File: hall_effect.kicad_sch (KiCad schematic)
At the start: 0 parts

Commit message: added MCU decaps and hall effect schematic
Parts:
- added R3 (x2), R4 (x2): 1.9k, symbol Device:R
- added R5, R6: 22k, symbol Device:R
- added R7: 1k, symbol Device:R
- added R8: 3.6k, symbol Device:R
- added U2, U4: OPA196xDGK, Package_SO:VSSOP-8_3x3mm_P0.65mm, symbol Amplifier_Operational:OPA196xDGK
- added U3: SM351LT, Package_TO_SOT_SMD:SOT-23, symbol Sensor_Magnetic:SM351LT
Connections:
- new net: R7.2, R8.2, U4.2 (-)
- new net: R3.1, R5.2, R6.1
- new net: R3.1, R3.2, U2.2 (-)
- new net: R4.1, R4.1, U2.3 (+)
- new net: R3.2, U2.6, U4.3 (+)
- new net: R4.2, U3.2 (OUTPUT)
- new net +3.3V: R5.1, U3.1 (VCC)
- new net +5V: U2.7 (V+), U4.7 (V+)
- new net ADC_IN1: R8.1, U4.6
- new net GND: R4.2, R6.2, R7.1, U2.4 (V-), U3.3 (GND), U4.4 (V-)

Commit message: layout
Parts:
- R11: renamed from R3; footprint (none) -> Resistor_SMD:R_0805_2012Metric
- R12: renamed from R4; footprint (none) -> Resistor_SMD:R_0805_2012Metric
- R3, R4, R5, R6, R7, R8: footprint (none) -> Resistor_SMD:R_0805_2012Metric
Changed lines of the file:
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@@
 			)
 		)
-		(property "Footprint" ""
+		(property "Footprint" "Resistor_SMD:R_0805_2012Metric"
 			(at 161.29 82.042 90)
 			(effects
@@
 			)
 		)
-		(property "Footprint" ""
+		(property "Footprint" "Resistor_SMD:R_0805_2012Metric"
 			(at 75.692 87.63 90)
 			(effects
@@
 		(dnp no)
 		(fields_autoplaced yes)
-		(property "Reference" "R3"
+		(property "Reference" "R11"
 			(at 91.44 76.2 90)
 			(effects
@@
 			)
 		)
-		(property "Footprint" ""
+		(property "Footprint" "Resistor_SMD:R_0805_2012Metric"
 			(at 91.44 84.328 90)
 			(effects
@@
 			(project "senior_design"
 				(path "/35c074f0-8545-4dc1-a57d-3ef0bc7d9188/ce5cb751-dcc9-43da-9e85-60783f09935d"
-					(reference "R3")
+					(reference "R11")
 					(unit 1)
 				)
@@
 		(dnp no)
 		(fields_autoplaced yes)
-		(property "Reference" "R4"
+		(property "Reference" "R12"
 			(at 105.41 54.6099 0)
 			(effects
@@
 			)
 		)
-		(property "Footprint" ""
+		(property "Footprint" "Resistor_SMD:R_0805_2012Metric"
 			(at 104.648 55.88 90)
 			(effects
@@
 			(project "senior_design"
 				(path "/35c074f0-8545-4dc1-a57d-3ef0bc7d9188/ce5cb751-dcc9-43da-9e85-60783f09935d"
-					(reference "R4")
+					(reference "R12")
 					(unit 1)
 				)
@@
 			)
 		)
-		(property "Footprint" ""
+		(property "Footprint" "Resistor_SMD:R_0805_2012Metric"
 			(at 96.52 64.262 90)
 			(effects
@@
 			)
 		)
-		(property "Footprint" ""
+		(property "Footprint" "Resistor_SMD:R_0805_2012Metric"
 			(at 140.208 90.17 90)
 			(effects
@@
 			)
 		)
-		(property "Footprint" ""
+		(property "Footprint" "Resistor_SMD:R_0805_2012Metric"
 			(at 116.84 90.678 90)
 			(effects
@@
 			)
 		)
-		(property "Footprint" ""
+		(property "Footprint" "Resistor_SMD:R_0805_2012Metric"
 			(at 75.692 77.47 90)
 			(effects

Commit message: layout work
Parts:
- removed U3: SM351LT, Package_TO_SOT_SMD:SOT-23, symbol Sensor_Magnetic:SM351LT
- added J2: Conn_01x03_Pin, Connector_PinHeader_2.54mm:PinHeader_1x03_P2.54mm_Vertical, symbol Connector:Conn_01x03_Pin
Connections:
- net +3.3V: now also J2.1 (Pin_1)
- net GND: now also J2.3 (Pin_3)
- net at R4.2: now also J2.2 (Pin_2)
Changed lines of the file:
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@@
 	(wire
 		(pts
-			(xy 73.66 59.69) (xy 90.17 59.69)
+			(xy 67.31 52.07) (xy 67.31 57.15)
 		)
 		(stroke
@@
 	(wire
 		(pts
+			(xy 67.31 57.15) (xy 64.77 57.15)
+		)
+		(stroke
+			(width 0)
+			(type default)
+		)
+	)
+	(wire
+		(pts
 			(xy 138.43 93.98) (xy 138.43 96.52)
 		)
@@
 	(wire
 		(pts
-			(xy 58.42 50.8) (xy 58.42 52.07)
+			(xy 64.77 59.69) (xy 90.17 59.69)
 		)
 		(stroke
@@
 	(wire
 		(pts
-			(xy 58.42 67.31) (xy 58.42 69.85)
-		)
-		(stroke
-			(width 0)
-			(type default)
-		)
-	)
-	(wire
-		(pts
 			(xy 102.87 49.53) (xy 102.87 52.07)
 		)
@@
 	(wire
 		(pts
+			(xy 67.31 62.23) (xy 64.77 62.23)
+		)
+		(stroke
+			(width 0)
+			(type default)
+		)
+	)
+	(wire
+		(pts
 			(xy 100.33 66.04) (xy 102.87 66.04)
 		)
@@
 		(pts
 			(xy 100.33 88.9) (xy 113.03 88.9)
+		)
+		(stroke
+			(width 0)
+			(type default)
+		)
+	)
+	(wire
+		(pts
+			(xy 67.31 68.58) (xy 67.31 62.23)
 		)
 		(stroke
@@
 	(symbol
 		(lib_id "power:GND")
-		(at 58.42 69.85 0)
+		(at 67.31 68.58 0)
 		(unit 1)
 		(exclude_from_sim no)
@@
 		(fields_autoplaced yes)
 		(property "Reference" "#PWR027"
-			(at 58.42 76.2 0)
+			(at 67.31 74.93 0)
 			(effects
 				(font
@@
 		)
 		(property "Value" "GND"
-			(at 58.42 74.93 0)
+			(at 67.31 73.66 0)
 			(effects
 				(font
@@
 		)
 		(property "Footprint" ""
-			(at 58.42 69.85 0)
+			(at 67.31 68.58 0)
 			(effects
 				(font
@@
 		)
 		(property "Datasheet" ""
-			(at 58.42 69.85 0)
+			(at 67.31 68.58 0)
 			(effects
 				(font
@@
 		)
 		(property "Description" "Power symbol creates a global label with name \"GND\" , ground"
-			(at 58.42 69.85 0)
+			(at 67.31 68.58 0)
 			(effects
 				(font
@@
 	)
 	(symbol
+		(lib_id "Connector:Conn_01x03_Pin")
+		(at 59.69 59.69 0)
+		(unit 1)
+		(exclude_from_sim no)
+		(in_bom yes)
+		(on_board yes)
+		(dnp no)
+		(fields_autoplaced yes)
+		(property "Reference" "J2"
+			(at 60.325 52.07 0)
+			(effects
+				(font
+					(size 1.27 1.27)
+				)
+			)
+		)
+		(property "Value" "Conn_01x03_Pin"
+			(at 60.325 54.61 0)
+			(effects
+				(font
+					(size 1.27 1.27)
+				)
+			)
+		)
+		(property "Footprint" "Connector_PinHeader_2.54mm:PinHeader_1x03_P2.54mm_Vertical"
+			(at 59.69 59.69 0)
+			(effects
+				(font
+					(size 1.27 1.27)
+				)
+				(hide yes)
+			)
+		)
+		(property "Datasheet" "~"
+			(at 59.69 59.69 0)
+			(effects
+				(font
+					(size 1.27 1.27)
+				)
+				(hide yes)
+			)
+		)
+		(property "Description" "Generic connector, single row, 01x03, script generated"
+			(at 59.69 59.69 0)
+			(effects
+				(font
+					(size 1.27 1.27)
+				)
+				(hide yes)
+			)
+		)
+		(pin "3"
+		)
+		(pin "1"
+		)
+		(pin "2"
+		)
+		(instances
+			(project ""
+				(path "/35c074f0-8545-4dc1-a57d-3ef0bc7d9188/ce5cb751-dcc9-43da-9e85-60783f09935d"
+					(reference "J2")
+					(unit 1)
+				)
+			)
+		)
+	)
+	(symbol
 		(lib_id "Device:R")
 		(at 102.87 55.88 180)
@@
 	)
 	(symbol
-		(lib_id "Sensor_Magnetic:SM351LT")
-		(at 63.5 59.69 0)
-		(unit 1)
-		(exclude_from_sim no)
-		(in_bom yes)
-		(on_board yes)
-		(dnp no)
-		(fields_autoplaced yes)
-		(property "Reference" "U3"
-			(at 54.61 58.4199 0)
-			(effects
-				(font
-					(size 1.27 1.27)
-				)
-				(justify right)
-			)
-		)
-		(property "Value" "SM351LT"
-			(at 54.61 60.9599 0)
-			(effects
-				(font
-					(size 1.27 1.27)
-				)
-				(justify right)
-			)
-		)
-		(property "Footprint" "Package_TO_SOT_SMD:SOT-23"
-			(at 62.23 59.69 0)
-			(effects
-				(font
-					(size 1.27 1.27)
-				)
-				(hide yes)
-			)
-		)
-		(property "Datasheet" "https://sensing.honeywell.com/honeywell-sensing-nanopower-series-product-sheet-50095501-a-en.pdf"
-			(at 62.23 59.69 0)
-			(effects
-				(font
-					(size 1.27 1.27)
-				)
-				(hide yes)
-			)
-		)
-		(property "Description" "Hall Effect Switch, SOT-23"
-			(at 63.5 59.69 0)
-			(effects
-				(font
-					(size 1.27 1.27)
-				)
-				(hide yes)
-			)
-		)
-		(pin "2"
-		)
-		(pin "1"
-		)
-		(pin "3"
-		)
-		(instances
-			(project ""
-				(path "/35c074f0-8545-4dc1-a57d-3ef0bc7d9188/ce5cb751-dcc9-43da-9e85-60783f09935d"
-					(reference "U3")
-					(unit 1)
-				)
-			)
-		)
-	)
-	(symbol
 		(lib_id "Amplifier_Operational:OPA196xDGK")
 		(at 151.13 71.12 0)
@@
 	(symbol
 		(lib_id "power:+3.3V")
-		(at 58.42 50.8 0)
+		(at 67.31 52.07 0)
 		(unit 1)
 		(exclude_from_sim no)
@@
 		(fields_autoplaced yes)
 		(property "Reference" "#PWR026"
-			(at 58.42 54.61 0)
+			(at 67.31 55.88 0)
 			(effects
 				(font
@@
 		)
 		(property "Value" "+3.3V"
-			(at 58.42 45.72 0)
+			(at 67.31 46.99 0)
 			(effects
 				(font
@@
 		)
 		(property "Footprint" ""
-			(at 58.42 50.8 0)
+			(at 67.31 52.07 0)
 			(effects
 				(font
@@
 		)
 		(property "Datasheet" ""
-			(at 58.42 50.8 0)
+			(at 67.31 52.07 0)
 			(effects
 				(font
@@
 		)
 		(property "Description" "Power symbol creates a global label with name \"+3.3V\""
-			(at 58.42 50.8 0)
-			(effects
-				(font
+			(at 67.31 52.07 0)
+			(effects
+				(font

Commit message: Updated Schematic
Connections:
- net GND: now also J2.2 (Pin_2); no longer J2.3 (Pin_3)
- net at R4.2: now also J2.3 (Pin_3); no longer J2.2 (Pin_2)
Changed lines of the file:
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@@
+	(wire
+		(pts
+			(xy 73.66 54.61) (xy 73.66 59.69)
+		)
+		(stroke
+			(width 0)
+			(type default)
+		)
+	)
 	(wire
 		(pts
@@
 	(wire
 		(pts
+			(xy 90.17 62.23) (xy 90.17 66.04)
+		)
+		(stroke
+			(width 0)
+			(type default)
+		)
+	)
+	(wire
+		(pts
 			(xy 121.92 68.58) (xy 125.73 68.58)
 		)
@@
 	(wire
 		(pts
-			(xy 64.77 59.69) (xy 90.17 59.69)
+			(xy 64.77 59.69) (xy 73.66 59.69)
 		)
 		(stroke
@@
 	(wire
 		(pts
-			(xy 67.31 62.23) (xy 64.77 62.23)
+			(xy 64.77 62.23) (xy 90.17 62.23)
 		)
 		(stroke
@@
 		(pts
 			(xy 100.33 88.9) (xy 113.03 88.9)
-		)
-		(stroke
-			(width 0)
-			(type default)
-		)
-	)
-	(wire
-		(pts
-			(xy 67.31 68.58) (xy 67.31 62.23)
-		)
-		(stroke
-			(width 0)
-			(type default)
-		)
-	)
-	(wire
-		(pts
-			(xy 90.17 59.69) (xy 90.17 66.04)
 		)
 		(stroke
@@
 	(symbol
 		(lib_id "power:GND")
-		(at 67.31 68.58 0)
+		(at 73.66 54.61 180)
 		(unit 1)
 		(exclude_from_sim no)
@@
 		(fields_autoplaced yes)
 		(property "Reference" "#PWR027"
-			(at 67.31 74.93 0)
+			(at 73.66 48.26 0)
 			(effects
 				(font
@@
 		)
 		(property "Value" "GND"
-			(at 67.31 73.66 0)
+			(at 73.66 49.53 0)
 			(effects
 				(font
@@
 		)
 		(property "Footprint" ""
-			(at 67.31 68.58 0)
+			(at 73.66 54.61 0)
 			(effects
 				(font
@@
 		)
 		(property "Datasheet" ""
-			(at 67.31 68.58 0)
+			(at 73.66 54.61 0)
 			(effects
 				(font
@@
 		)
 		(property "Description" "Power symbol creates a global label with name \"GND\" , ground"
-			(at 67.31 68.58 0)
-			(effects
-				(font
+			(at 73.66 54.61 0)
+			(effects
+				(font

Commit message: Updated Schematic
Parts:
- added D10, D9: PESD3V3S1UL, Diode_SMD:D_SOD-882, symbol Diode:PESD3V3S1UL
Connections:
- net at J2.3 (Pin_3), R4.2: now also D9.1 (K)
- net +3.3V renamed VDDA
- net VDDA: now also D10.1 (K)
- net GND renamed GNDA
- net GNDA: now also D10.2 (A), D9.2 (A)

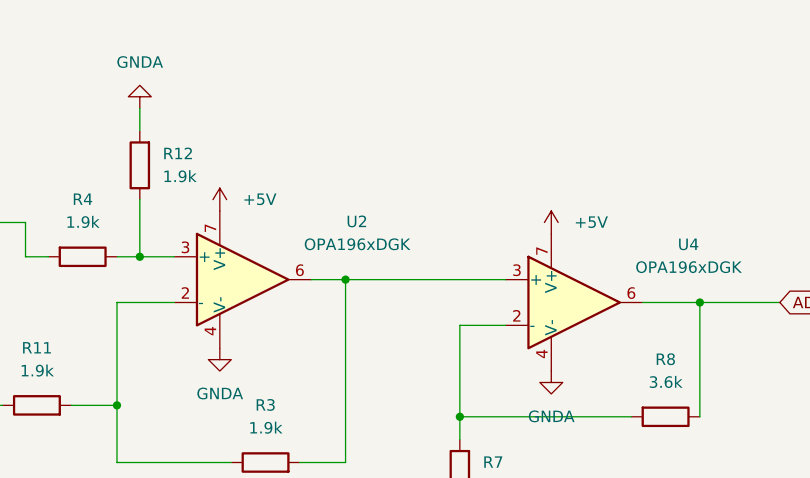
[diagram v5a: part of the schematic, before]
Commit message: rearranged HE and SD, added analog power plane
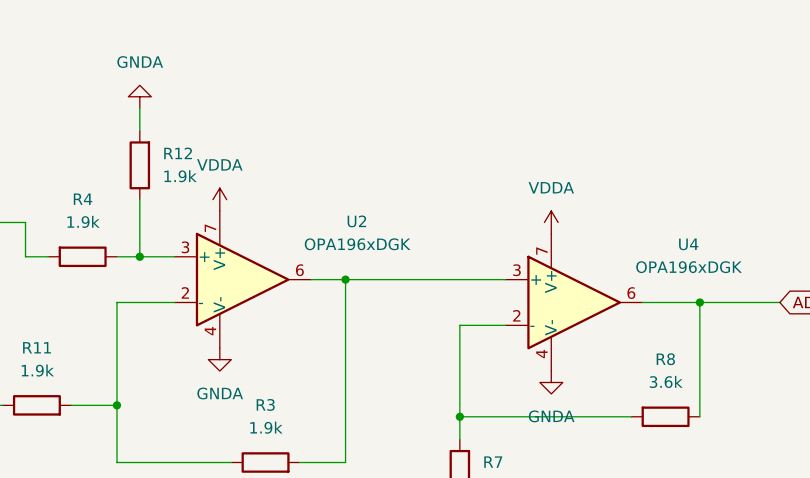
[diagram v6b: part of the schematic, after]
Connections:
- net +5V is gone; now on net VDDA: U2.7 (V+), U4.7 (V+)

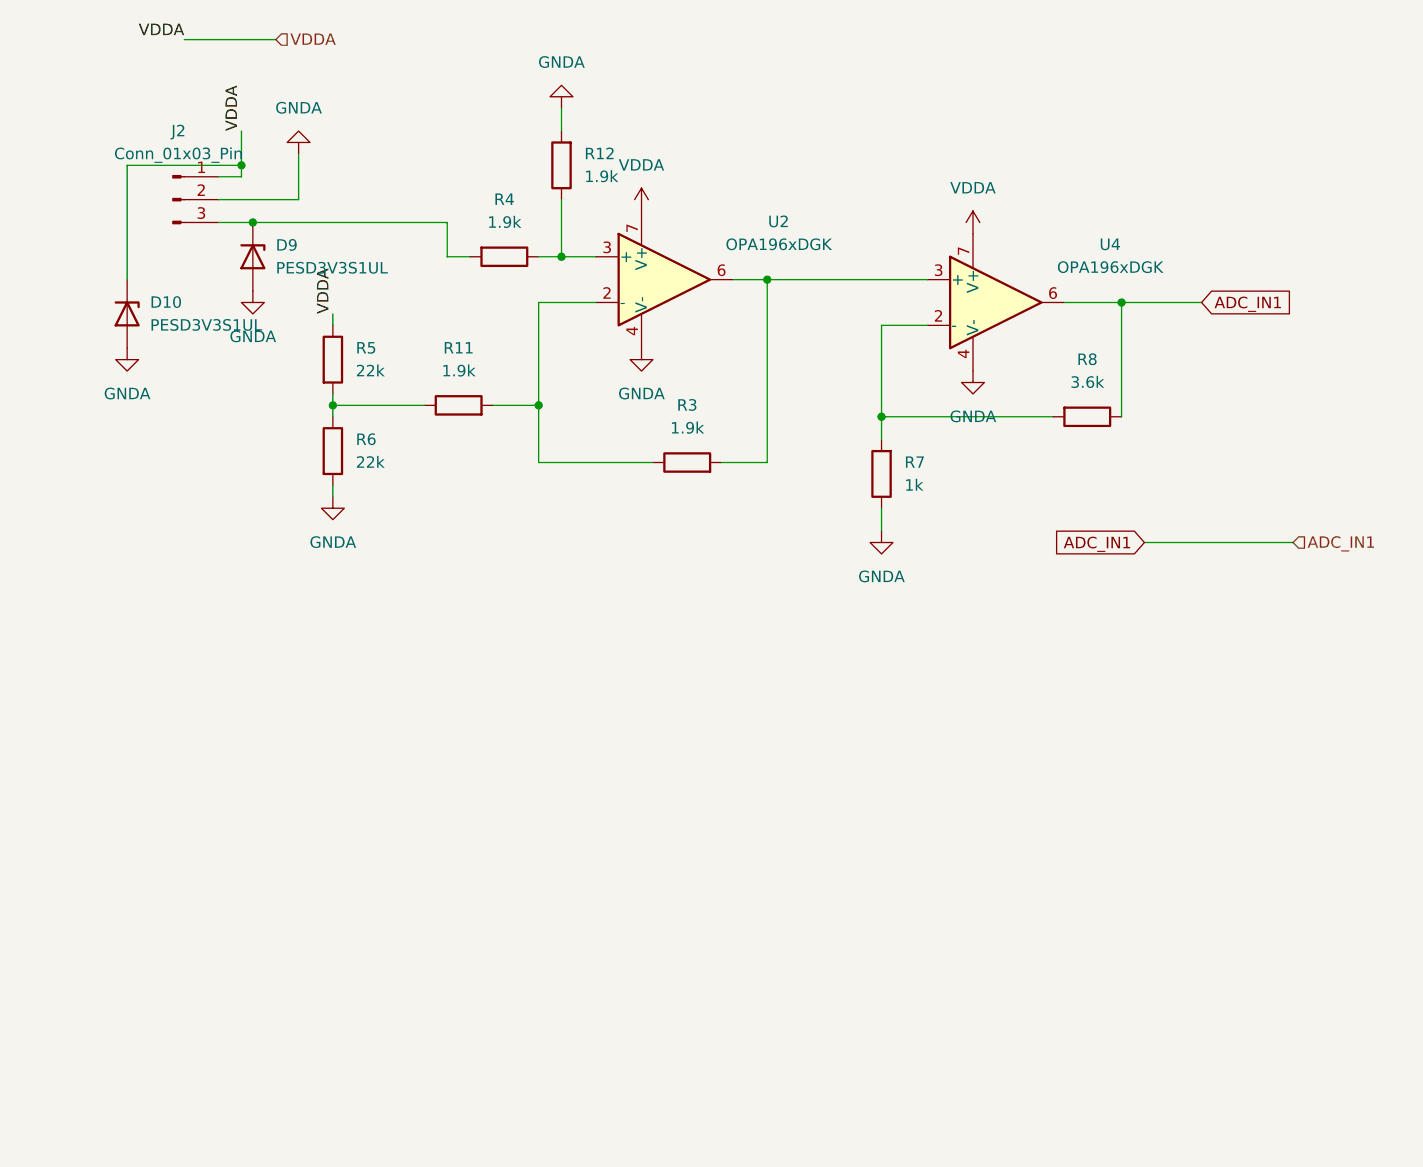
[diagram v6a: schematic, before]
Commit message: added HE2 and expanded VDDA plane
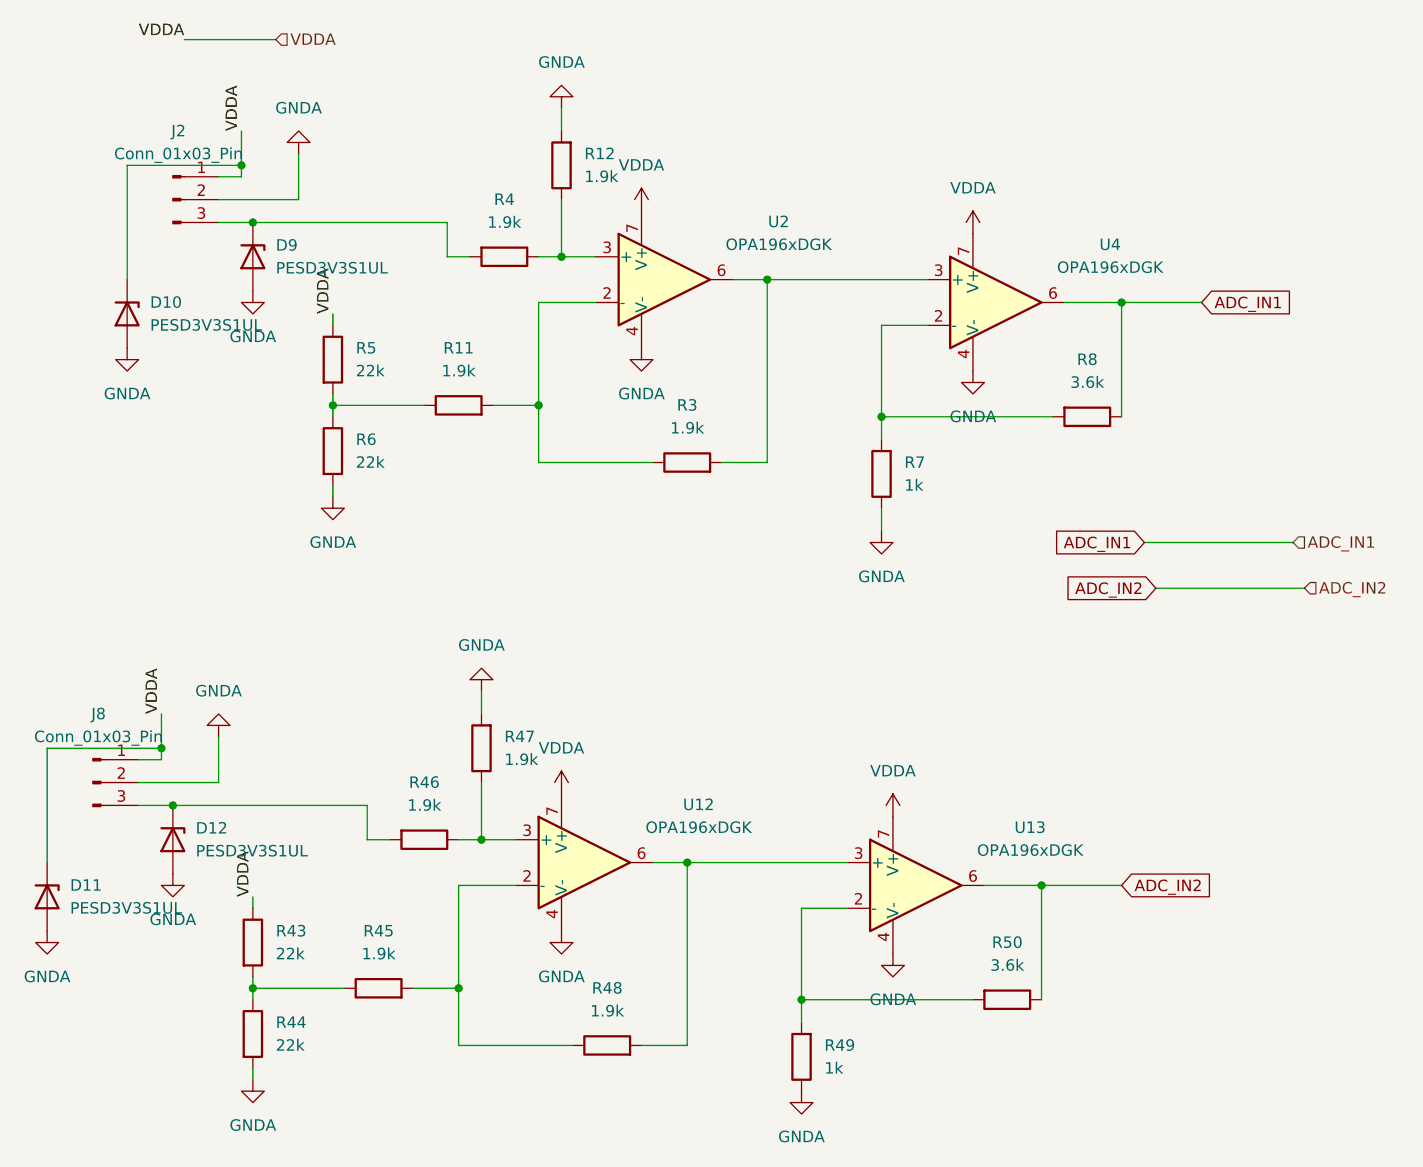
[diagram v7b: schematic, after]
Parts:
- added D11, D12: PESD3V3S1UL, Diode_SMD:D_SOD-882, symbol Diode:PESD3V3S1UL
- added J8: Conn_01x03_Pin, Connector_PinHeader_2.54mm:PinHeader_1x03_P2.54mm_Vertical, symbol Connector:Conn_01x03_Pin
- added R43, R44: 22k, Resistor_SMD:R_0805_2012Metric, symbol Device:R
- added R45, R46, R47, R48: 1.9k, Resistor_SMD:R_0805_2012Metric, symbol Device:R
- added R49: 1k, Resistor_SMD:R_0805_2012Metric, symbol Device:R
- added R50: 3.6k, Resistor_SMD:R_0805_2012Metric, symbol Device:R
- added U12, U13: OPA196xDGK, Package_SO:VSSOP-8_3x3mm_P0.65mm, symbol Amplifier_Operational:OPA196xDGK
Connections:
- net GNDA: now also D11.2 (A), D12.2 (A), J8.2 (Pin_2), R44.2, R47.2, R49.1, U12.4 (V-), U13.4 (V-)
- net VDDA: now also D11.1 (K), J8.1 (Pin_1), R43.1, U12.7 (V+), U13.7 (V+)
- new net: R43.2, R44.1, R45.1
- new net: D12.1 (K), J8.3 (Pin_3), R46.2
- new net: R45.2, R48.1, U12.2 (-)
- new net: R48.2, U12.6, U13.3 (+)
- new net: R49.2, R50.2, U13.2 (-)
- new net: R46.1, R47.1, U12.3 (+)
- new net ADC_IN2: R50.1, U13.6
